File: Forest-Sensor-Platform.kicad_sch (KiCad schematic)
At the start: 69 parts, among them J1 USB_C_2.0_16P, J10 I2C2, J3 MSD-1-A, J4 POWER, J7 Conn_01x06 2.54mm Screw Termi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, J8 I2C1, J9 SWD, SW1 WIO_RST, U10 TLV75733PDRV, U11 TPS613222ADBV, U13 TPS22991CRAAR, U2 LM66200DRLR, U3 Wio-E5, STM32WLE5 Module, U6 TPT482-VS2R, U7 TPS22991CRAAR, U8 LM66200DRLR

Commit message: Swap to module for ch
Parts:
- removed J9: SWD, Connector_JST:JST_SH_BM04B-SRSS-TB_1x04-1MP_P1.00mm_Vertical, symbol Connector_Generic_Shielded:Conn_01x04_Shielded
- added J2: Conn_01x05_Shielded, Connector_JST:JST_SH_BM05B-SRSS-TB_1x05-1MP_P1.00mm_Vertical, symbol Connector_Generic_Shielded:Conn_01x05_Shielded
- added U4: (no value), CH572D:CH572D-Module, symbol buck-wio:CH572D_Module
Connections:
- net +3.3V: now also J2.3 (Pin_3)
- net +5V: now also U2.2 (VOUT), U2.7 (VOUT), U4.9 (5V)
- net D+: now also U4.5 (D+)
- net D-: now also U4.6 (D-)
- net GND: now also J2.4 (Pin_4), U4.10 (GND), U4.11 (GND)
- net SWD-WIO-CLK: now also J2.1 (Pin_1), U4.3 (SWDCLK)
- net SWD-WIO-IO: now also J2.2 (Pin_2), U4.1 (SWDIO)
- net UART-WIO-RX: now also U4.7 (UART_TX)
- net UART-WIO-TX: now also U4.8 (UART_RX)
- net WIO-RST: now also J2.5 (Pin_5), U4.2 (SWDRST)
- net at R22.1, U7.2 (ON): now also U4.4 (GPIO_EN)

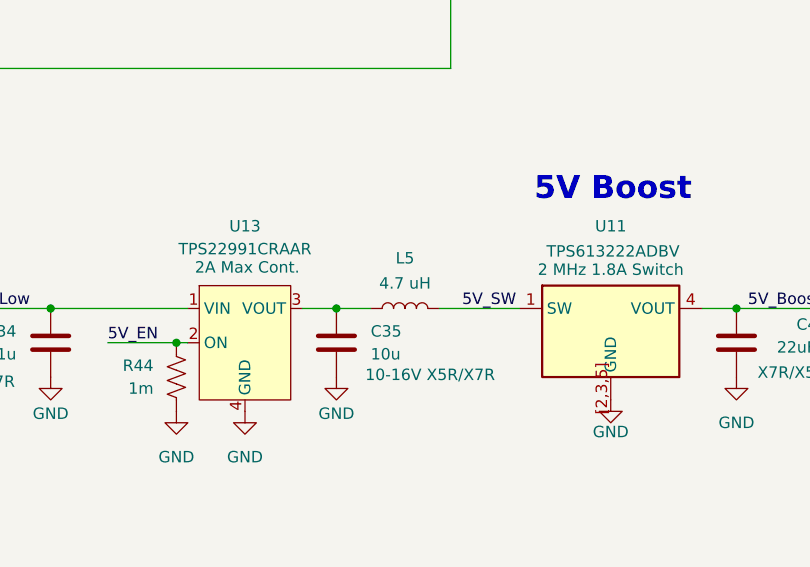
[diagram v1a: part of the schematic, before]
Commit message: Add ch module 3D model
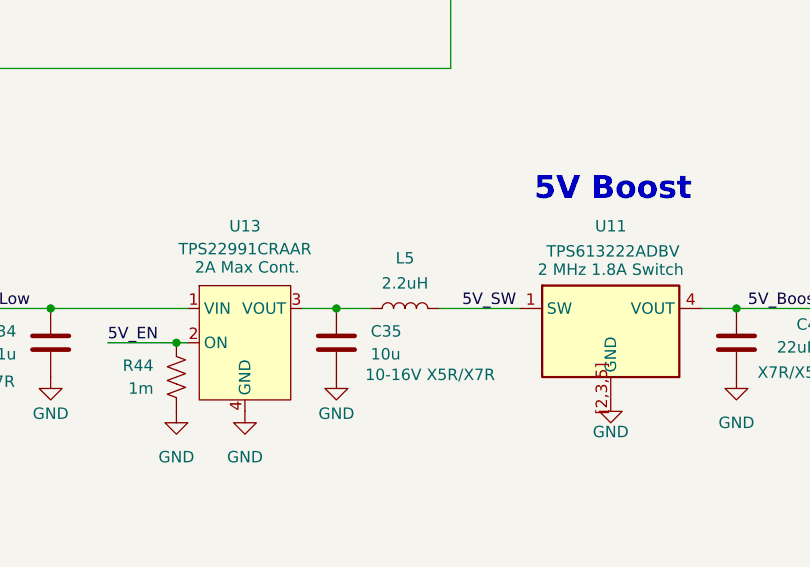
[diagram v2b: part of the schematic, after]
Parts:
- L5: value 4.7 uH -> 2.2uH
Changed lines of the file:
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@@
 			)
 		)
-		(property "Value" "4.7 uH"
+		(property "Value" "2.2uH"
 			(at 189.23 248.666 90)
 			(show_name no)

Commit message: Fix net problems
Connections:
- net Receiver_Input_Enable: now also R37.1, U3.25 (PB9), U6.2 (RE); no longer R36.1, U3.21 (PA9), U6.4 (D)
- net Receiver_Output_Enable: now also R36.1, U3.21 (PA9); no longer R37.1, U3.25 (PB9)
- net UART-1-TX: now also U6.4 (D); no longer U6.2 (RE)
- net Battery_Shunt_Low renamed Battery_Out
- net VSENSE_VOUT renamed VSENSE_OUT

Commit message: Fix DRC errors
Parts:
- C10, C15, C44: Digi-Key PN (none) -> 311-1344-2-ND; MANUFACTURER (none) -> YAGEO; MPN (none) -> CC0603KRX7R9BB104
- C12, C14: Digi-Key PN (none) -> 399-C0805C105K3RACTUTR-ND; MANUFACTURER (none) -> KEMET; MPN (none) -> C0805C105K3RACTU
- C13, C9: value 10uF 50V -> 10uF 25V; Digi-Key PN (none) -> 490-12323-2-ND; MANUFACTURER (none) -> Murata Electronics; MPN (none) -> GRT188R61E106ME13D
- C16, C19, C21, C32: value 100n -> 100nF 50V; Digi-Key PN (none) -> 311-1344-2-ND; MANUFACTURER (none) -> YAGEO; MPN (none) -> CC0603KRX7R9BB104
- C30, C34: value 1u -> 1uF 25V; Digi-Key PN (none) -> 445-6931-2-ND; MANUFACTURER (none) -> TDK; MPN (none) -> CGA3E1X7R1E105K080AC
- C31, C35: value 10u -> 10uF 25V; Digi-Key PN (none) -> 490-12323-2-ND; MANUFACTURER (none) -> Murata Electronics; MPN (none) -> GRT188R61E106ME13D
- C46: value 22uF 10V -> 22uF 16V; Digi-Key PN (none) -> 1276-7076-2-ND; MANUFACTURER (none) -> Samsung Electro-Mechanics; MPN (none) -> CL10A226MO7JZNC
- D12, D2, D6: Digi-Key PN (none) -> 160-1435-2-ND; MANUFACTURER (none) -> Lite-On Inc.; MPN (none) -> LTST-C190KGKT
- D7: Digi-Key PN (none) -> SMAJ5.0CALFTR-ND; MANUFACTURER (none) -> Littelfuse Inc.; MPN (none) -> SMAJ5.0CA
- J1, J3: MANUFACTURER (none) -> Same Sky; Manufacturer Same Sky -> (none)
- J10, J8: symbol Connector_Generic_Shielded:Conn_01x04_Shielded -> Connector_Generic_MountingPin:Conn_01x04_MountingPin; Digi-Key PN (none) -> 455-BM04B-SRSS-TBTR-ND; MANUFACTURER (none) -> JST Sales America Inc.; MPN (none) -> BM04B-SRSS-TB
- J2: symbol Connector_Generic_Shielded:Conn_01x05_Shielded -> Connector_Generic_MountingPin:Conn_01x05_MountingPin; Digi-Key PN (none) -> 455-BM05B-SRSS-TBTR-ND; MANUFACTURER (none) -> JST Sales America Inc.; MPN (none) -> BM05B-SRSS-TB
- J4: Digi-Key PN (none) -> 952-2262-ND; MANUFACTURER (none) -> Harwin Inc.; MPN (none) -> M20-9990246
- J7: MANUFACTURER (none) -> On Shore Technology Inc.; Manufacturer On Shore Technology Inc. -> (none)
- L5: MANUFACTURER (none) -> Abracon LLC; Manufacturer Abracon LLC -> (none)
- R13, R16, R17, R18, R29, R30: Digi-Key PN (none) -> RMCF0603FT10K0TR-ND; MANUFACTURER (none) -> Stackpole Electronics Inc; MPN (none) -> RMCF0603FT10K0
- R21, R22, R31, R36, R37, R44: value 1m -> 1M; Digi-Key PN (none) -> RMCF0603FT1M00TR-ND; MANUFACTURER (none) -> Stackpole Electronics Inc; MPN (none) -> RMCF0603FT1M00
- R25, R26: Digi-Key PN (none) -> RMCF0603FT5K10TR-ND; MANUFACTURER (none) -> Stackpole Electronics Inc; MPN (none) -> RMCF0603FT5K10
- R27, R28: Digi-Key PN (none) -> RMCF0603FT4K70TR-ND; MANUFACTURER (none) -> Stackpole Electronics Inc; MPN (none) -> RMCF0603FT4K70
- R33: value DNP -> 0; Digi-Key PN (none) -> RMCF0805ZT0R00CT-ND; MANUFACTURER (none) -> Stackpole Electronics Inc; MPN (none) -> RMCF0805ZT0R00; now not fitted
- R34: MANUFACTURER (none) -> Stackpole Electronics Inc; Manufacturer Stackpole Electronics Inc -> (none)
- R38, R39, R40: value TBD -> 1K; Digi-Key PN (none) -> RMCF0603FT1K00TR-ND; MANUFACTURER (none) -> Stackpole Electronics Inc; MPN (none) -> RMCF0603FT1K00
- R42, R43: Digi-Key PN (none) -> RMCF0603ZT0R00TR-ND; MANUFACTURER (none) -> Stackpole Electronics Inc; MPN (none) -> RMCF0603ZT0R00
- SMA1: Digi-Key PN (none) -> SAM8857-ND; MANUFACTURER (none) -> Samtec Inc.; MPN (none) -> SMA-J-P-H-ST-EM1
- SW1: Digi-Key PN 2073-SWT0210-045026GSACT-ND -> 108-PTS647SK38SMTR2LFSTR-ND; MANUFACTURER (none) -> C&K; MPN SWT0210-045026GSA -> PTS647SK38SMTR2 LFS; Manufacturer GCT -> (none)
- U10, U11, U13, U2, U7, U8: MANUFACTURER (none) -> Texas Instruments; Manufacturer Texas Instruments -> (none)
- U3: Digi-Key PN (none) -> 1597-317990829TR-ND; MANUFACTURER (none) -> Seeed Technology Co., Ltd; MPN (none) -> LoRa-E5-HF
- U4: value (none) -> CH572D Module; MANUFACTURER (none) -> Nanjing Qinheng Microelectronics (WCH); MPN (none) -> CH572D
- U6: MANUFACTURER (none) -> 3PEAK; Manufacturer 3PEAK -> (none)
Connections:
- net Batt_Out is gone; now on net Battery_Out: U8.6 (VIN2)
- net GND: now also U10.[2,3,5,7] (GND); no longer U10.[2,3,5] (GND)
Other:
- note added: "RS422/485"
- note removed: "RS422/482"
- moved on the sheet: D2, J1, R13, R21, R25, R26, TP1, TP2, U10, U2, U4

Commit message: Add USB controller back
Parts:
- removed U4: CH572D Module, CH572D:CH572D-Module, symbol buck-wio:CH572D_Module
- added R35: 100, Resistor_SMD:R_0805_2012Metric_Pad1.20x1.40mm_HandSolder, symbol Device:R_US
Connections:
- net at C44.1, D7.2 (A2), R33.2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: now also R35.2; no longer J7.1 (Pin_1)
- net USB_VOUT_EN: now reaches R22.1, U7.2 (ON)
- new net: J7.1 (Pin_1), R35.1
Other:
- note added: "Boost converter Shut-off"
- note added: "Duplex select tie"
- note added: "INPUT: 5V Boost OUTPUT: TO -> USB"
- note added: "INPUT: USB or 5V Boost OUTPUT: USB Controller"
- note added: "Software controlled supply for device. Out to USB for host mode"
- note removed: "Duplex select"
- note removed: "Out to USB for host mode"
- moved on the sheet: C10, C12, C13, C14, C15, C16, C19, C21, C30, C31, C32, C34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

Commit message: V1 final
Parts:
- C34: value 1uF 25V -> 1u
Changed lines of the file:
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@@
 			)
 		)
-		(property "Value" "1uF 25V"
+		(property "Value" "1u"
 			(at 41.91 223.5199 0)
 			(show_name no)
